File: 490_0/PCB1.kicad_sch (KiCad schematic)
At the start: 1 part, among them J11 Conn_01x08

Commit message: Changed 8conn and BOM update
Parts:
- J11: footprint *CapStone*:CONN_S8B-XH-A_JST -> *CapStone*:CONN_S08B-XASK-1_JST; Digikey Link https://www.digikey.ca/en/products/detail/jst-sales-america-inc/S8B-XH-A/1651023 -> https://www.digikey.ca/en/products/detail/jst-sales-america-inc/s08b-xask-1/2621356; Manufacturer Part S8B-XH-A -> S08B-XASK-1; Package (none) -> Bulk; Price 0.33 -> 0.81; Supplier P/N 455-S8B-XH-A-ND -> 455-S08B-XASK-1-ND; Type Through Hole -> Through Hole, Right Angle
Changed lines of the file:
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@@
 			)
 		)
-		(property "Footprint" "*CapStone*:CONN_S8B-XH-A_JST"
+		(property "Footprint" "*CapStone*:CONN_S08B-XASK-1_JST"
 			(at 256.54 23.495 0)
 			(effects
@@
 			)
 		)
-		(property "Datasheet" "kicad-embed://B3B-XH-A.pdf"
+		(property "Datasheet" "kicad-embed://eXA-WB-new.pdf"
 			(at 256.54 30.48 0)
 			(effects
@@
 			)
 		)
-		(property "Digikey Link" "https://www.digikey.ca/en/products/detail/jst-sales-america-inc/S8B-XH-A/1651023"
+		(property "Digikey Link" "https://www.digikey.ca/en/products/detail/jst-sales-america-inc/s08b-xask-1/2621356"
 			(at 256.54 35.56 0)
 			(effects
@@
 			)
 		)
-		(property "Manufacturer Part" "S8B-XH-A"
+		(property "Manufacturer Part" "S08B-XASK-1"
 			(at 256.54 35.56 0)
 			(effects
@@
 			)
 		)
-		(property "Price" "0.33"
+		(property "Price" "0.81"
 			(at 256.54 35.56 0)
 			(effects
@@
 			)
 		)
-		(property "Supplier P/N" "455-S8B-XH-A-ND"
+		(property "Supplier P/N" "455-S08B-XASK-1-ND"
 			(at 256.54 35.56 0)
 			(effects
@@
 			)
 		)
-		(property "Type" "Through Hole"
+		(property "Type" "Through Hole, Right Angle"
 			(at 256.54 35.56 0)
 			(effects
@@
 			(at 256.54 35.56 0)
 			(effects
+				(font
+					(size 1.27 1.27)
+				)
+				(hide yes)
+			)
+		)
+		(property "Package" "Bulk"
+			(at 256.54 35.56 0)
+			(effects

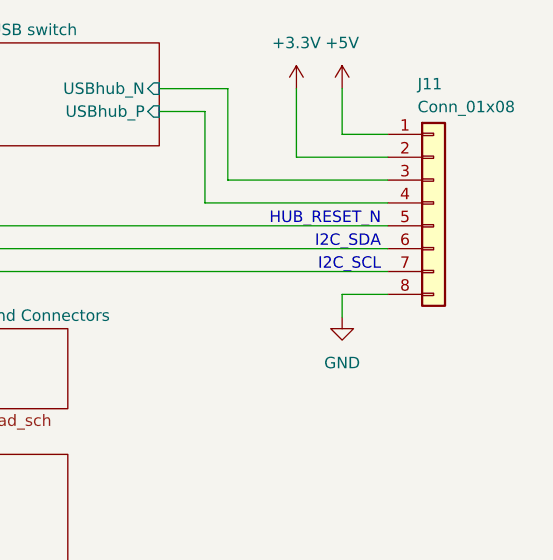
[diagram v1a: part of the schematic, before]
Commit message: Added seperate ground for PWM motors
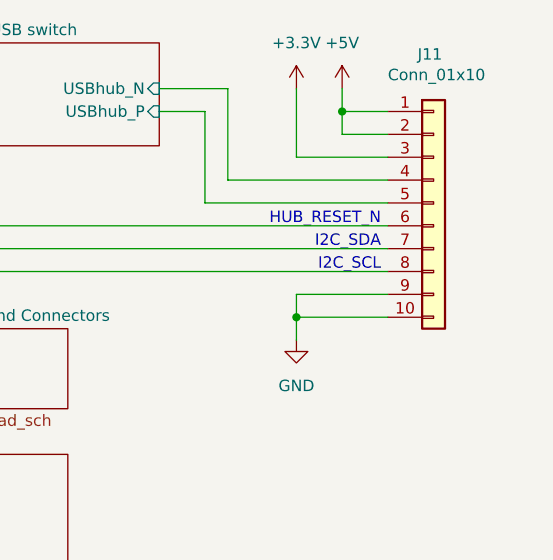
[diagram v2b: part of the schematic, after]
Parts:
- removed J11: Conn_01x08, *CapStone*:CONN_S08B-XASK-1_JST, symbol PCM_4ms_Connector:Conn_01x08
- added J11: Conn_01x10, symbol Connector_Generic:Conn_01x10
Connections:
- net +3.3V: now also J11.3 (Pin_3)
- net +5V: now also J11.1 (Pin_1), J11.2 (Pin_2)
- net GND: now also J11.10 (Pin_10), J11.9 (Pin_9)
- net PCB1-Board Connector A/GPIO13: now also J11.6 (Pin_6)
- net PCB1-Charging and Power Port + USB switch/USBhub_N: now also J11.4 (Pin_4)
- net PCB1-Charging and Power Port + USB switch/USBhub_P: now also J11.5 (Pin_5)
- net SCL1: now also J11.8 (Pin_8)
- net SDA1: now also J11.7 (Pin_7)

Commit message: Added 10 pin connector footprint
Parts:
- J11: footprint (none) -> Connector_JST:JST_XH_S10B-XH-A-1_1x10_P2.50mm_Horizontal
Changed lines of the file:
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@@
 			)
 		)
-		(property "Footprint" ""
+		(property "Footprint" "Connector_JST:JST_XH_S10B-XH-A-1_1x10_P2.50mm_Horizontal"
 			(at 256.54 35.56 0)
 			(effects

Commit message: Added side B for SW1
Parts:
- J11: symbol Connector_Generic:Conn_01x10 -> capstone_parts:Conn_01x10
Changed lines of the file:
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@@
 	)
 	(symbol
-		(lib_id "Connector_Generic:Conn_01x10")
+		(lib_id "capstone_parts:Conn_01x10")
 		(at 256.54 35.56 0)
 		(unit 1)

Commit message: Rerouted + external coponents update
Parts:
- removed J11: Conn_01x10, Connector_JST:JST_XH_S10B-XH-A-1_1x10_P2.50mm_Horizontal, symbol capstone_parts:Conn_01x10
- added J11: S3B-XH-A, Connector_JST:JST_XH_S3B-XH-A_1x03_P2.50mm_Horizontal, symbol capstone_parts:Conn_01x03
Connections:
- net +3.3V: now also J11.2 (Pin_2)
- net +5V: now also J11.3 (Pin_3)
- net GND: now also J11.1 (Pin_1)
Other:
- sheet PCB1-Board Connector A ports: added none; removed GPIO13
- sheet PCB1-ToF HDMI Connector ports: added USBhub_N, USBhub_P; removed none
- note removed: "HUB_RESET_N"
- note removed: "I2C_SCL"
- note removed: "I2C_SDA"

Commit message: Friday, March 20th: PCB Final for BOM
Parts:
- added H5, H6, H7, H8: MountingHole, MountingHole:MountingHole_3mm, symbol Mechanical:MountingHole
